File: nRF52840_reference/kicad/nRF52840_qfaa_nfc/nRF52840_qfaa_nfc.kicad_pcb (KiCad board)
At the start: 2 copper layers, 30 parts, among them J1 CONN_COAXIAL, U1 nRF52840, X1 XTAL_32MHZ, X2 XTAL_32KHZ

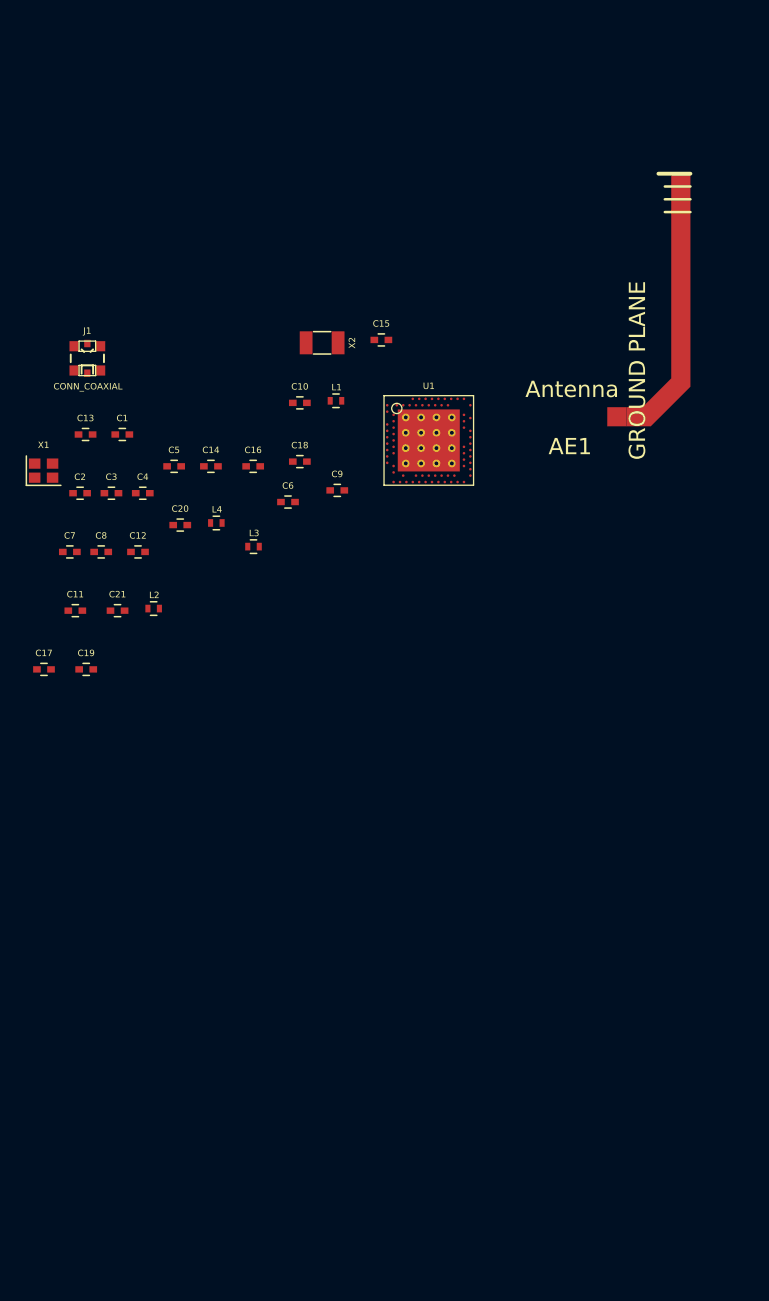
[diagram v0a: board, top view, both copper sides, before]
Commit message: Update KiCAD project nRF52840_qfaa_nfc
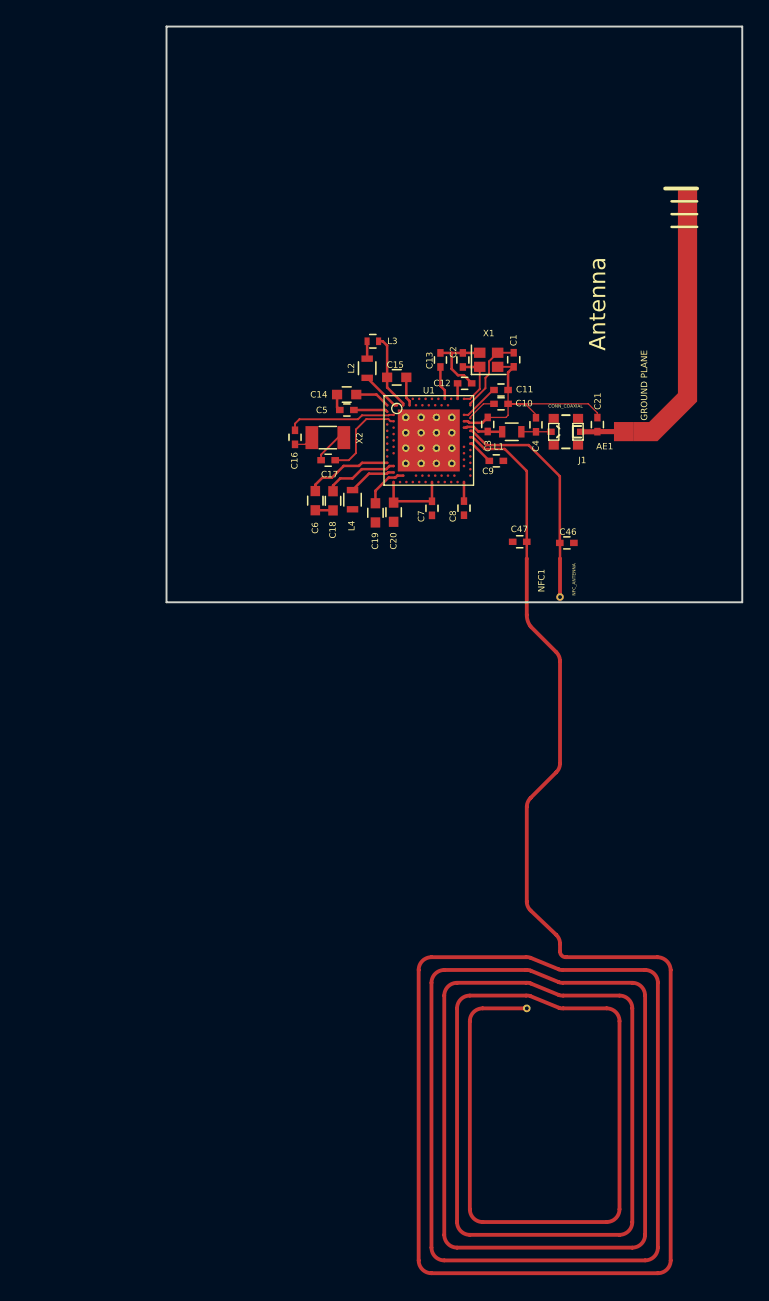
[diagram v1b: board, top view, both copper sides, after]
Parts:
- added C46: 300pF, Nordic_misc:C_0402, F.Cu at (111.3, 105.4)
- added C47: 300pF, Nordic_misc:C_0402, F.Cu at (107.6, 105.3)
- added NFC1: NFC_ANTENNA, Nordic_misc:Nordic_misc-NFC_ANT, F.Cu at (110.8, 106.6)
- C1, C16, C17, C2: value C -> 12pF
- C10, C13, C9: value C -> N.C
- C11: value C -> 100pF
- C12, C5, C7, C8: value C -> 100nF
- C14, C15: value C -> 1.0uF; footprint Nordic_misc:C_0402 -> Nordic_misc:C_0603
- C18, C19, C20, C6: value C -> 4.7uF; footprint Nordic_misc:C_0402 -> Nordic_misc:C_0603
- C21: value C -> 1.2pF
- C3: value C -> 0.8pF
- C4: value C -> 0.5pF
- L1: value L -> 3.3nH; footprint Nordic_misc:L_0402 -> Nordic_misc:L_0603
- L2, L4: value L -> 10uH; footprint Nordic_misc:L_0402 -> Nordic_misc:L_0603
- L3: value L -> 15nH
- moved C21 40.2 mm to (113.7, 96.1), turned to 270 degrees
- moved J1 37.8 mm to (111.2, 96.7), turned to 90 degrees
- moved C11 37.5 mm to (106.1, 93.4), turned to 180 degrees
- moved X1 35.8 mm to (105.2, 91.0)
- moved C2 31.7 mm to (103.2, 91.1), turned to 270 degrees
- moved C4 31.2 mm to (108.9, 96.1), turned to 270 degrees
- moved C1 31.1 mm to (107.1, 91.0), turned to 90 degrees
- moved C3 29.9 mm to (105.1, 96.1), turned to 270 degrees
- moved C12 28.7 mm to (103.3, 92.9)
- moved C8 28.6 mm to (103.3, 102.6), turned to 270 degrees
- moved C7 28.5 mm to (100.7, 102.7), turned to 270 degrees
- moved C13 28.3 mm to (101.4, 91.1), turned to 90 degrees
- moved C17 27.6 mm to (92.6, 98.9), turned to 180 degrees
- moved C19 25.7 mm to (96.3, 103.0), turned to 270 degrees
- moved L2 25.1 mm to (95.7, 91.7), turned to 270 degrees
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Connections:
- C18 pad 1: GND -> VDD
- C18 pad 2: VDD -> GND
- C19 pad 1: GND -> Net-(C19-Pad1)
- C19 pad 2: Net-(C19-Pad2) -> GND
- C20 pad 1: GND -> +3V3
- C20 pad 2: +3V3 -> GND
- C6 pad 1: GND -> +3V3
- C6 pad 2: +3V3 -> GND
- C7 pad 1: GND -> +3V3
- C7 pad 2: +3V3 -> GND
- C8 pad 1: GND -> +3V3
- C8 pad 2: +3V3 -> GND
- C9 pad 1: GND -> Net-(C9-Pad1)
- C9 pad 2: Net-(C9-Pad2) -> GND
- U1 pad A10: /P0.29 -> (no net)
- U1 pad A12: /P0.02 -> (no net)
- U1 pad A14: /P1.15 -> (no net)
- U1 pad A16: /P1.13 -> (no net)
- U1 pad A20: /P1.10 -> (no net)
- U1 pad A8: /P0.31 -> (no net)
- U1 pad AA24: /SWDCLK -> (no net)
- U1 pad AC11: /P0.16 -> (no net)
- U1 pad AC13: /P0.18/RESET -> (no net)
- U1 pad AC15: /P0.19 -> (no net)
- U1 pad AC17: /P0.21 -> (no net)
- U1 pad AC19: /P0.23 -> (no net)
- U1 pad AC21: /P0.25 -> (no net)
- U1 pad AC24: /SWDIO -> (no net)
- U1 pad AC5: Net-(C19-Pad2) -> Net-(C19-Pad1)
- U1 pad AC9: /P0.14 -> (no net)
- U1 pad AD10: /P0.15 -> (no net)
- U1 pad AD12: /P0.17 -> (no net)
- U1 pad AD16: /P0.20 -> (no net)
- U1 pad AD18: /P0.22 -> (no net)
- U1 pad AD20: /P0.24 -> (no net)
- U1 pad AD22: /P1.00 -> (no net)
- U1 pad AD4: /D- -> (no net)
- U1 pad AD6: /D+ -> (no net)
- U1 pad AD8: /P0.13 -> (no net)
- U1 pad B11: /P0.28 -> (no net)
- U1 pad B13: /P0.03 -> (no net)
- U1 pad B15: /P1.14 -> (no net)
- U1 pad B17: /P1.12 -> (no net)
- U1 pad B19: /P1.11 -> (no net)
- U1 pad B9: /P0.30 -> (no net)
- U1 pad G1: /P0.26 -> (no net)
- U1 pad H2: /P0.27 -> (no net)
- U1 pad J1: /P0.04/AIN2 -> (no net)
- U1 pad J24: /P0.10 -> /NFC2
- U1 pad K2: /P0.05/AIN3 -> (no net)
- U1 pad L1: /P0.06 -> (no net)
- U1 pad L24: /P0.09 -> /NFC1
- U1 pad M2: /P0.07 -> (no net)
- U1 pad N1: /P0.08 -> (no net)
- U1 pad N24: Net-(C9-Pad2) -> Net-(C9-Pad1)
- U1 pad P2: /P1.08 -> (no net)
- U1 pad P23: /P1.07 -> (no net)
- U1 pad R1: /P1.09 -> (no net)
- U1 pad R24: /P1.06 -> (no net)
- U1 pad T2: /P0.11 -> (no net)
- U1 pad T23: /P1.05 -> (no net)
- U1 pad U1: /P0.12 -> (no net)
- U1 pad U24: /P1.04 -> (no net)
- U1 pad V23: /P1.03 -> (no net)
- U1 pad W24: /P1.02 -> (no net)
- U1 pad Y23: /P1.01 -> (no net)
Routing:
- net GND: track 0.00 -> 30.7 mm
- net +3V3: track 0.00 -> 18.6 mm
- net /NFC2: track 0.00 -> 14.9 mm
- net /NFC1: track 0.00 -> 12.4 mm
- net Net-(C16-Pad1): track 0.00 -> 8.53 mm
- net Net-(C17-Pad1): track 0.00 -> 7.09 mm
- net Net-(C1-Pad2): track 0.00 -> 6.24 mm
- net VDD: track 0.00 -> 6.18 mm
- net Net-(C15-Pad1): track 0.00 -> 5.99 mm
- net Net-(C2-Pad2): track 0.00 -> 4.61 mm
- net Net-(L4-Pad2): track 0.00 -> 3.78 mm
- net Net-(C19-Pad1): track 0.00 -> 3.64 mm
- net Net-(L2-Pad2): track 0.00 -> 3.54 mm
- net Net-(AE1-Pad1): track 0.00 -> 3.37 mm
- net Net-(C3-Pad2): track 0.00 -> 3.20 mm
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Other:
- board outline added: 45 x 45 mm
- net class Default: clearance 0.2 -> 0.1
- rule trace_clearance: 0.2 -> 0.1
- rule trace_min: 0.2 -> 0.1

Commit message: Update KiCAD Project nRF52840_qfaa_nfc
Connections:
- U1 pad 74: Net-(U1-Pad74) -> GND
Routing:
- net GND: track 30.7 -> 37.5 mm
